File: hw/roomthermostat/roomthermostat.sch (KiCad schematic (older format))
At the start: 9 parts, among them U1 TSIC206_SOIC8

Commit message: created 3d images, schematics and gerber files for roomthermostat
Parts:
- C1, C2: symbol C -> standard:C
- LOGO1: symbol OPEN_HARDWARE_1 -> logo:OPEN_HARDWARE_1
- MOD1: symbol bus-module_atmega328 -> modules:bus-module_atmega328
- MOD2: symbol Graphic-OLED-Display_4wireSPI -> display:Graphic-OLED-Display_4wireSPI
- S1, S2, S3: symbol PushButton_SPST_NO -> standard:PushButton_SPST_NO
- U1: symbol TSIC206_SOIC8 -> sensors:TSIC206_SOIC8
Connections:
- wire segments 48 -> 60
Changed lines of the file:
@@
-EESchema Schematic File Version 2
-LIBS:display
-LIBS:modules
-LIBS:power
-LIBS:sensors
-LIBS:standard
-LIBS:transistors
-LIBS:logo
+EESchema Schematic File Version 4
 LIBS:roomthermostat-cache
-EELAYER 25 0
+EELAYER 26 0
 EELAYER END
 $Descr A4 11693 8268
@@
 $EndDescr
 $Comp
-L bus-module_atmega328 MOD1
+L modules:bus-module_atmega328 MOD1
 U 1 1 5B2200B5
 P 5100 4000
@@
 	5300 5050 5300 5150
 Wire Wire Line
-	5300 5150 4900 5150
+	5300 5150 5200 5150
 Connection ~ 5000 5150
 Connection ~ 5200 5150
@@
 Connection ~ 5100 5150
 $Comp
-L GND #PWR01
+L power:GND #PWR01
 U 1 1 5B22013D
 P 5100 5250
@@
 $EndComp
 $Comp
-L VCC #PWR02
+L power:VCC #PWR02
 U 1 1 5B220159
 P 5100 2800
@@
 	4900 3000 4900 2900
 Wire Wire Line
-	4900 2900 5300 2900
+	4900 2900 5000 2900
 Wire Wire Line
 	5300 2900 5300 3000
@@
 Connection ~ 5200 2900
 $Comp
-L TSIC206_SOIC8 U1
+L sensors:TSIC206_SOIC8 U1
 U 1 1 5B2201B8
 P 8200 3350
@@
 $EndComp
 $Comp
-L Graphic-OLED-Display_4wireSPI MOD2
+L display:Graphic-OLED-Display_4wireSPI MOD2
 U 1 1 5B220AD1
 P 6900 3750
@@
 $EndComp
 $Comp
-L C C1
+L standard:C C1
 U 1 1 5B220C28
 P 6450 4050
@@
 $EndComp
 $Comp
-L C C2
+L standard:C C2
 U 1 1 5B220CB9
 P 7900 4050
@@
 	6700 3850 6450 3850
 Wire Wire Line
-	6600 3750 6600 4350
+	6600 3750 6600 4250
 Wire Wire Line
 	8100 3850 7900 3850
 Wire Wire Line
-	7900 2850 7900 3950
-Wire Wire Line
-	8300 3750 8300 4350
-$Comp
-L GND #PWR03
+	7900 2850 7900 3850
+Wire Wire Line
+	8300 3750 8300 4250
+$Comp
+L power:GND #PWR03
 U 1 1 5B221010
 P 6600 4350
@@
 $EndComp
 $Comp
-L GND #PWR04
+L power:GND #PWR04
 U 1 1 5B22102E
 P 8300 4350
@@
 $EndComp
 $Comp
-L VCC #PWR05
+L power:VCC #PWR05
 U 1 1 5B22104C
 P 7900 2850
@@
 $EndComp
 $Comp
-L VCC #PWR06
+L power:VCC #PWR06
 U 1 1 5B22106A
 P 6450 2850
@@
 /DISP_CS
 Wire Wire Line
-	6450 2850 6450 3950
+	6450 2850 6450 3850
 Connection ~ 6450 3850
 Wire Wire Line
@@
 	8500 5500 8500 4100
 Wire Bus Line
-	6900 4300 7300 4300
-Wire Bus Line
 	7300 4300 7300 5500
 Entry Wire Line
@@
 Entry Wire Line
 	6050 4650 6150 4750
-Wire Bus Line
-	6150 3900 6150 5500
 Wire Bus Line
 	4100 5500 8500 5500
@@
 NoConn ~ 5650 3700
 $Comp
-L PushButton_SPST_NO S1
+L standard:PushButton_SPST_NO S1
 U 1 1 5B221710
 P 3850 3100
@@
 $EndComp
 $Comp
-L PushButton_SPST_NO S2
+L standard:PushButton_SPST_NO S2
 U 1 1 5B22176B
 P 3850 3350
@@
 $EndComp
 $Comp
-L PushButton_SPST_NO S3
+L standard:PushButton_SPST_NO S3
 U 1 1 5B22178E
 P 3850 3600
@@
 	3850 3100 3750 3100
 Wire Wire Line
-	3750 3100 3750 3700
+	3750 3100 3750 3350
 Wire Wire Line
 	3850 3600 3750 3600
@@
 Connection ~ 3750 3350
 $Comp
-L GND #PWR07
+L power:GND #PWR07
 U 1 1 5B221CED
 P 3750 3700
@@
 Entry Wire Line
 	4100 4550 4200 4450
-Wire Bus Line
-	4100 4100 4100 5500
 NoConn ~ 4550 3700
 NoConn ~ 4550 3800
@@
 NoConn ~ 4550 4650
 $Comp
-L OPEN_HARDWARE_1 LOGO1
+L logo:OPEN_HARDWARE_1 LOGO1
 U 1 1 5B225797
 P 3250 5700
@@
 	1    0    0    -1
 $EndComp
+Wire Wire Line
+	5000 5150 4900 5150
+Wire Wire Line
+	5200 5150 5100 5150
+Wire Wire Line
+	5100 5150 5000 5150
+Wire Wire Line
+	5100 2900 5200 2900
+Wire Wire Line
+	5000 2900 5100 2900
+Wire Wire Line
+	5200 2900 5300 2900
+Wire Wire Line
+	6450 3850 6450 3950
+Wire Wire Line
+	6600 4250 6600 4350
+Wire Wire Line
+	7900 3850 7900 3950
+Wire Wire Line
+	8300 4250 8300 4350
+Wire Wire Line
+	3750 3600 3750 3700
+Wire Wire Line
+	3750 3350 3750 3600
+Wire Bus Line
+	4100 4100 4100 5500
+Wire Bus Line
+	6900 4300 7300 4300
+Wire Bus Line
+	6150 3900 6150 5500
 $EndSCHEMATC

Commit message: make roomthermostat compatible to bus-module_atmega328 rev A and rev B
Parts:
- removed MOD1: bus-module_atmega328, Modules:bus-module_atmega328, symbol modules:bus-module_atmega328
- added MOD1: bus-module_atmega328_revB, Modules:bus-module_atmega328, symbol modules:bus-module_atmega328_revB
- LOGO1: footprint (none) -> Symbol:Symbol_OSHW-Logo_Copper
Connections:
- wire segments 60 -> 56
- no-connect marks 13 -> 15
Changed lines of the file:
@@
 Sheet 1 1
 Title "roomthermostat"
-Date "2018-06-14"
-Rev "1"
+Date "2018-09-22"
+Rev "A"
 Comp "koewiba"
 Comment1 ""
@@
 Comment4 ""
 $EndDescr
-$Comp
-L modules:bus-module_atmega328 MOD1
-U 1 1 5B2200B5
-P 5100 4000
-F 0 "MOD1" H 4950 3850 50  0000 C CNN
-F 1 "bus-module_atmega328" V 5200 4000 40  0000 C CNN
-F 2 "Modules:bus-module_atmega328" H 5100 3850 60  0001 C CNN
-F 3 "" H 5100 3850 60  0000 C CNN
-	1    5100 4000
-	1    0    0    -1
-$EndComp
 Wire Wire Line
 	4900 5050 4900 5150
@@
 P 5100 2800
 F 0 "#PWR02" H 5100 2975 50  0001 C CNN
-F 1 "VCC" H 5100 2900 50  0000 C CNN
+F 1 "VCC" H 5100 2925 50  0000 C CNN
 F 2 "" H 5100 2800 60  0001 C CNN
 F 3 "" H 5100 2800 60  0001 C CNN
@@
 $EndComp
 Wire Wire Line
-	4900 3000 4900 2900
-Wire Wire Line
-	4900 2900 5000 2900
-Wire Wire Line
 	5300 2900 5300 3000
 Wire Wire Line
 	5100 2800 5100 2900
-Connection ~ 5100 2900
-Wire Wire Line
-	5000 3000 5000 2900
-Connection ~ 5000 2900
 Wire Wire Line
 	5200 3000 5200 2900
@@
 P 7900 2850
 F 0 "#PWR05" H 7900 3025 50  0001 C CNN
-F 1 "VCC" H 7900 2950 50  0000 C CNN
+F 1 "VCC" H 7900 2975 50  0000 C CNN
 F 2 "" H 7900 2850 60  0001 C CNN
 F 3 "" H 7900 2850 60  0001 C CNN
@@
 P 6450 2850
 F 0 "#PWR06" H 6450 3025 50  0001 C CNN
-F 1 "VCC" H 6450 2950 50  0000 C CNN
+F 1 "VCC" H 6450 2975 50  0000 C CNN
 F 2 "" H 6450 2850 60  0001 C CNN
 F 3 "" H 6450 2850 60  0001 C CNN
@@
 F 0 "LOGO1" H 3250 5975 50  0000 C CNN
 F 1 "OPEN_HARDWARE_1" H 3250 5475 25  0000 C CNN
-F 2 "" H 3250 5700 60  0001 C CNN
+F 2 "Symbol:Symbol_OSHW-Logo_Copper" H 3250 5700 60  0001 C CNN
 F 3 "" H 3250 5700 60  0001 C CNN
 	1    3250 5700
@@
 	5100 2900 5200 2900
 Wire Wire Line
-	5000 2900 5100 2900
-Wire Wire Line
 	5200 2900 5300 2900
 Wire Wire Line
@@
 Wire Wire Line
 	3750 3350 3750 3600
+$Comp
+L modules:bus-module_atmega328_revB MOD1
+U 1 1 5BA6C4B8
+P 5100 4000
+F 0 "MOD1" H 5100 4100 40  0000 C CNN
+F 1 "bus-module_atmega328_revB" H 5100 3875 40  0000 C CNN
+F 2 "Modules:bus-module_atmega328" H 5100 3850 60  0001 C CNN
+F 3 "" H 5100 3850 60  0000 C CNN
+	1    5100 4000
+	1    0    0    -1
+$EndComp
+NoConn ~ 5000 3000
+NoConn ~ 4900 3000
 Wire Bus Line
 	4100 4100 4100 5500

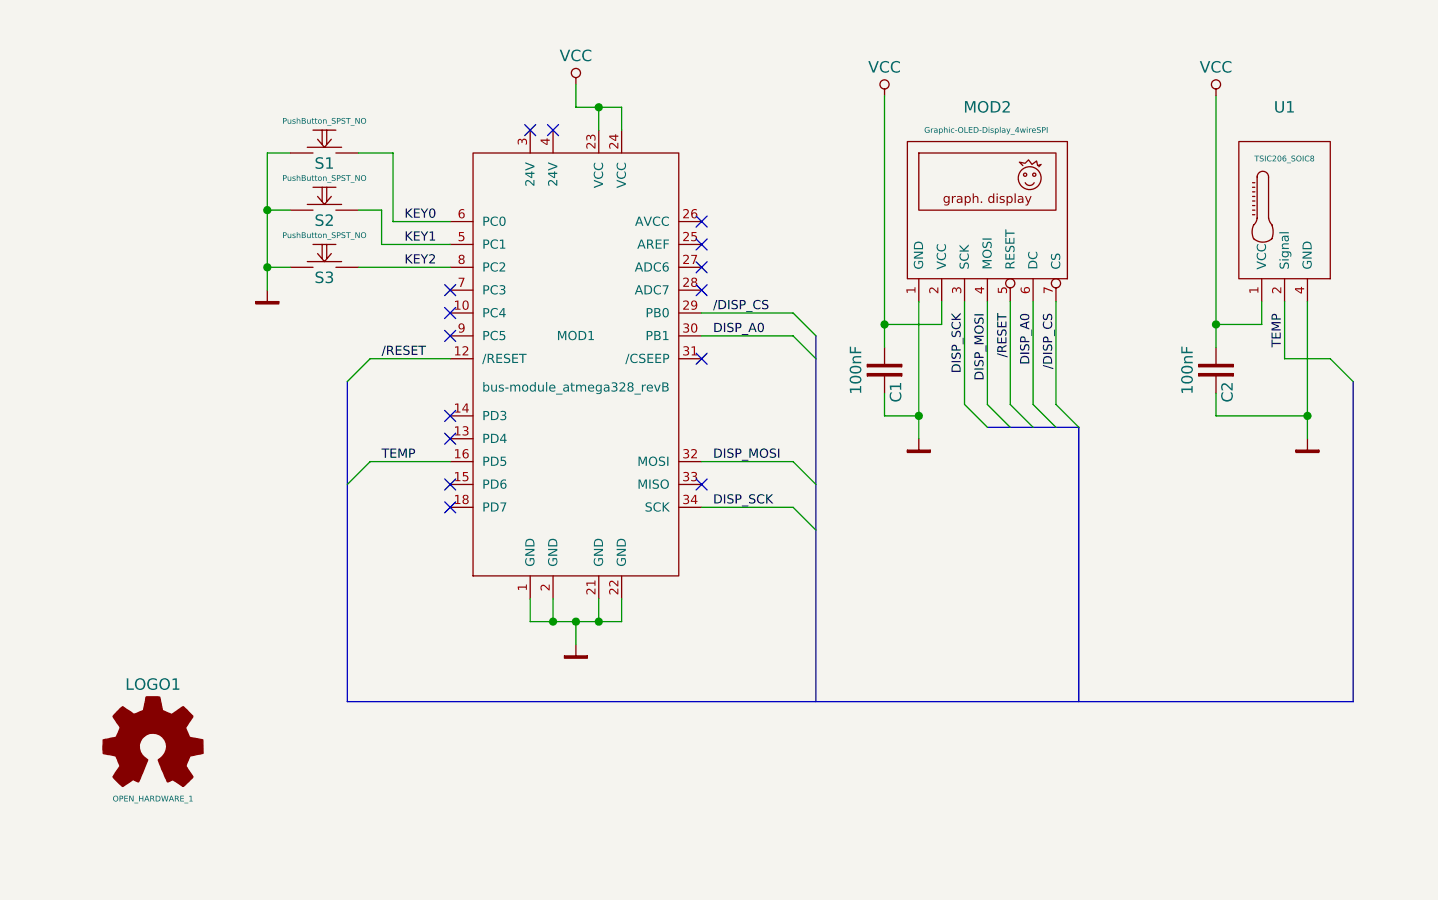
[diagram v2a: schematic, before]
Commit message: Change pin-assignment of display and temp.sensor
* bumped revision to rev B
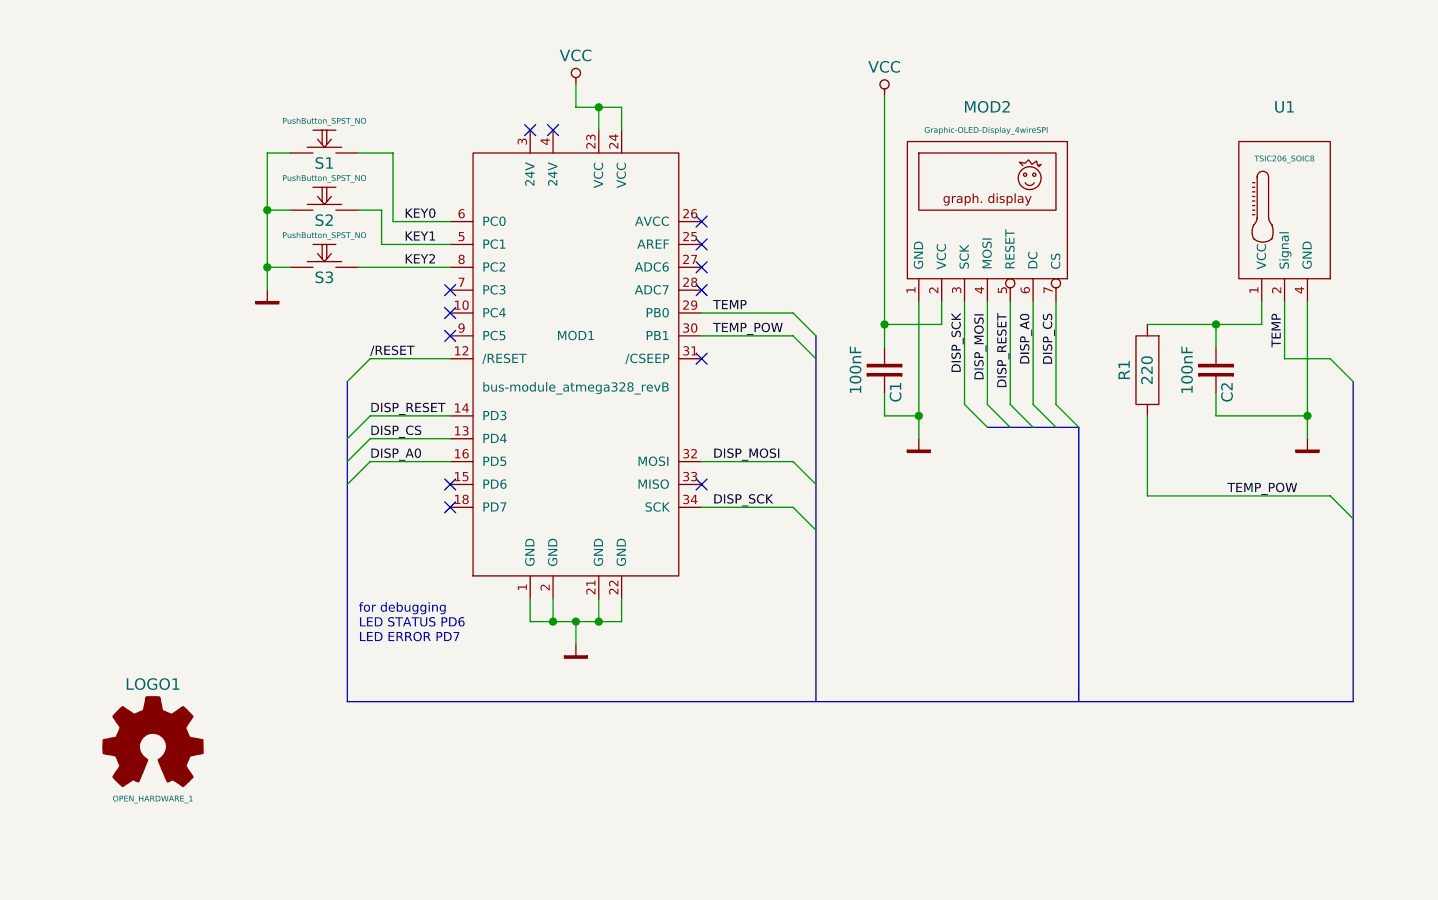
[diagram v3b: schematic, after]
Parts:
- added R1: 220, Resistor:R_0805, symbol standard:R
- S1, S2, S3: footprint Switch_Miscelleaneus:PHAP3301 -> Switch_Miscelleaneus:PushButton_SPST_SMD_JTP-1138_BacksideMount
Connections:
- net /RESET: no longer MOD2.5 (RESET)
- net DISP_A0: now also MOD1.16 (PD5); no longer MOD1.30 (PB1)
- net TEMP: now also MOD1.29 (PB0); no longer MOD1.16 (PD5)
- net VCC: no longer C2.1, U1.1 (VCC)
- net DISP_CS: now reaches MOD1.13 (PD4)
- net DISP_CS: now also MOD2.7 (CS)
- net DISP_RESET: now reaches MOD1.14 (PD3)
- net DISP_RESET: now also MOD2.5 (RESET)
- removed net /DISP_CS: MOD1.29 (PB0), MOD2.7 (CS)
- new net: C2.1, R1.1, U1.1 (VCC)
- new net TEMP_POW: MOD1.30 (PB1), R1.2
- no-connect marks 15 -> 13
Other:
- note added: "for debugging\nLED STATUS PD6\nLED ERROR PD7"
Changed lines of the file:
@@
 Sheet 1 1
 Title "roomthermostat"
-Date "2018-09-22"
-Rev "A"
+Date "2019-03-05"
+Rev "B"
 Comp "koewiba"
 Comment1 ""
@@
 Text Label 5700 4650 0    40   ~ 0
 DISP_SCK
-Text Label 5700 3800 0    40   ~ 0
-/DISP_CS
-Text Label 5700 3900 0    40   ~ 0
+Text Label 4200 4350 0    40   ~ 0
+DISP_CS
+Text Label 4200 4450 0    40   ~ 0
 DISP_A0
 Wire Wire Line
@@
 Wire Wire Line
 	5650 3800 6050 3800
-Text Label 4250 4000 0    40   ~ 0
+Text Label 4200 4000 0    40   ~ 0
 /RESET
 Wire Wire Line
@@
 Wire Wire Line
 	8100 3850 7900 3850
-Wire Wire Line
-	7900 2850 7900 3850
 Wire Wire Line
 	8300 3750 8300 4250
@@
 $EndComp
 $Comp
-L power:VCC #PWR05
-U 1 1 5B22104C
-P 7900 2850
-F 0 "#PWR05" H 7900 3025 50  0001 C CNN
-F 1 "VCC" H 7900 2975 50  0000 C CNN
-F 2 "" H 7900 2850 60  0001 C CNN
-F 3 "" H 7900 2850 60  0001 C CNN
-	1    7900 2850
-	1    0    0    -1
-$EndComp
-$Comp
 L power:VCC #PWR06
 U 1 1 5B22106A
@@
 DISP_MOSI
 Text Label 7000 3800 3    40   ~ 0
-/RESET
+DISP_RESET
 Text Label 7100 3800 3    40   ~ 0
 DISP_A0
 Text Label 7200 3800 3    40   ~ 0
-/DISP_CS
+DISP_CS
 Wire Wire Line
 	6450 2850 6450 3850
@@
 Wire Wire Line
 	8100 3750 8100 3850
-Connection ~ 7900 3850
 Wire Wire Line
 	7900 4150 7900 4250
@@
 Wire Wire Line
 	8200 4000 8400 4000
-Wire Bus Line
-	8500 5500 8500 4100
 Wire Bus Line
 	7300 4300 7300 5500
@@
 F 0 "S1" H 4000 3025 50  0000 C BNN
 F 1 "PushButton_SPST_NO" H 4000 3225 25  0000 C BNN
-F 2 "Switch_Miscelleaneus:PHAP3301" H 3850 3100 60  0001 C CNN
+F 2 "Switch_Miscelleaneus:PushButton_SPST_SMD_JTP-1138_BacksideMount" H 3850 3100 60  0001 C CNN
 F 3 "" H 3850 3100 60  0000 C CNN
 	1    3850 3100
@@
 F 0 "S2" H 4000 3275 50  0000 C BNN
 F 1 "PushButton_SPST_NO" H 4000 3475 25  0000 C BNN
-F 2 "Switch_Miscelleaneus:PHAP3301" H 3850 3350 60  0001 C CNN
+F 2 "Switch_Miscelleaneus:PushButton_SPST_SMD_JTP-1138_BacksideMount" H 3850 3350 60  0001 C CNN
 F 3 "" H 3850 3350 60  0000 C CNN
 	1    3850 3350
@@
 F 0 "S3" H 4000 3525 50  0000 C BNN
 F 1 "PushButton_SPST_NO" H 4000 3725 25  0000 C BNN
-F 2 "Switch_Miscelleaneus:PHAP3301" H 3850 3600 60  0001 C CNN
+F 2 "Switch_Miscelleaneus:PushButton_SPST_SMD_JTP-1138_BacksideMount" H 3850 3600 60  0001 C CNN
 F 3 "" H 3850 3600 60  0000 C CNN
 	1    3850 3600
@@
 	1    0    0    -1
 $EndComp
-Text Label 4250 4450 0    40   ~ 0
+Text Label 5700 3800 0    40   ~ 0
 TEMP
 Wire Wire Line
@@
 NoConn ~ 4550 3800
 NoConn ~ 4550 3900
-NoConn ~ 4550 4250
-NoConn ~ 4550 4350
 NoConn ~ 4550 4550
 NoConn ~ 4550 4650
@@
 NoConn ~ 5000 3000
 NoConn ~ 4900 3000
+Text Label 4200 4250 0    40   ~ 0
+DISP_RESET
+Wire Wire Line
+	4550 4250 4200 4250
+Wire Wire Line
+	4550 4350 4200 4350
+Entry Wire Line
+	4100 4350 4200 4250
+Entry Wire Line
+	4100 4450 4200 4350
+Text Label 5700 3900 0    40   ~ 0
+TEMP_POW
+$Comp
+L standard:R R1
+U 1 1 5C7F083A
+P 7600 4050
+F 0 "R1" H 7600 3950 50  0000 C CNN
+F 1 "220" H 7600 4050 50  0000 C CNN
+F 2 "Resistor:R_0805" H 7600 4050 60  0001 C CNN
+F 3 "" H 7600 4050 60  0000 C CNN
+	1    7600 4050
+	0    1    1    0
+$EndComp
+Wire Wire Line
+	7600 3850 7900 3850
+Connection ~ 7900 3850
+Wire Wire Line
+	7600 4250 7600 4600
+Wire Wire Line
+	7600 4600 8400 4600
+Text Label 7950 4600 0    40   ~ 0
+TEMP_POW
+Entry Wire Line
+	8400 4600 8500 4700
+Text Notes 4150 5250 0    40   ~ 0
+for debugging\nLED STATUS PD6\nLED ERROR PD7
+Wire Bus Line
+	8500 4100 8500 5500
 Wire Bus Line
 	4100 4100 4100 5500
